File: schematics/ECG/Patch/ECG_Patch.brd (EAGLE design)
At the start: 15.7 x 26.7 mm, 10 parts

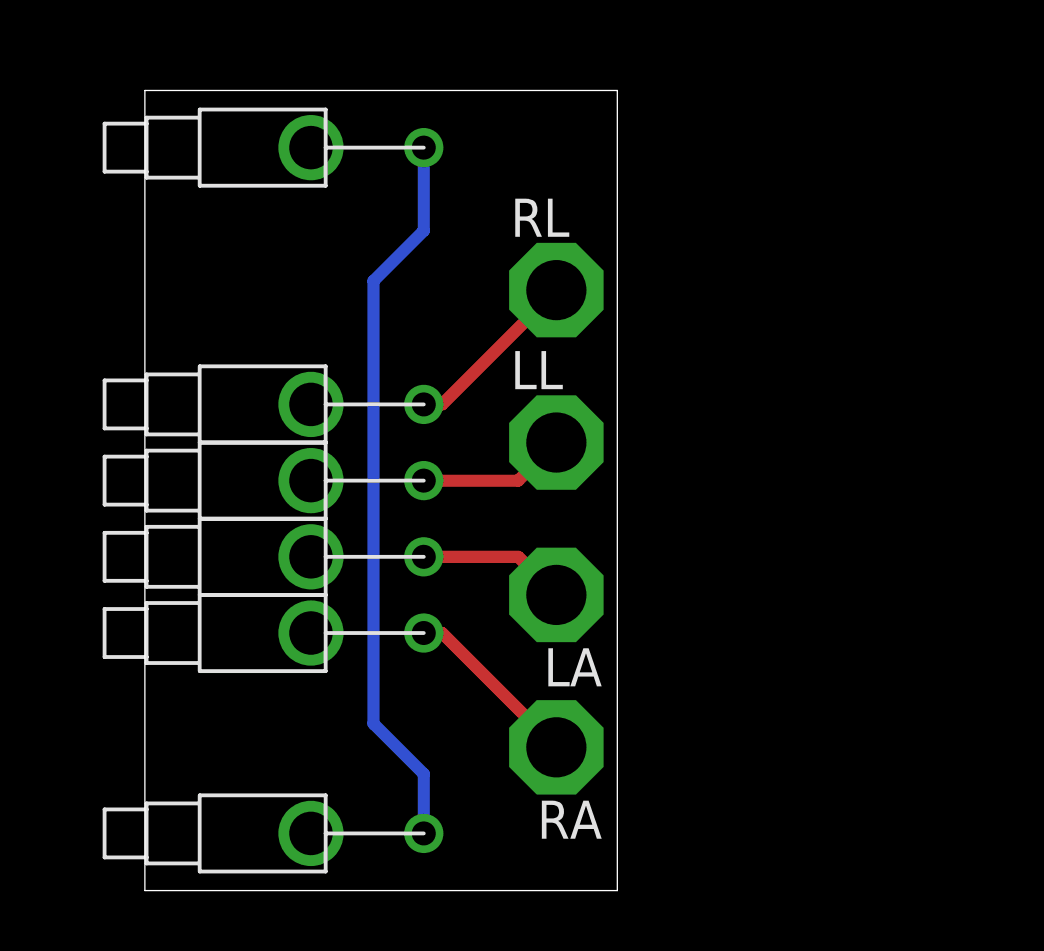
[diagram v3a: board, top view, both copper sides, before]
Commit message: updated all boards to slightly larger dimensions and new target/piston positions
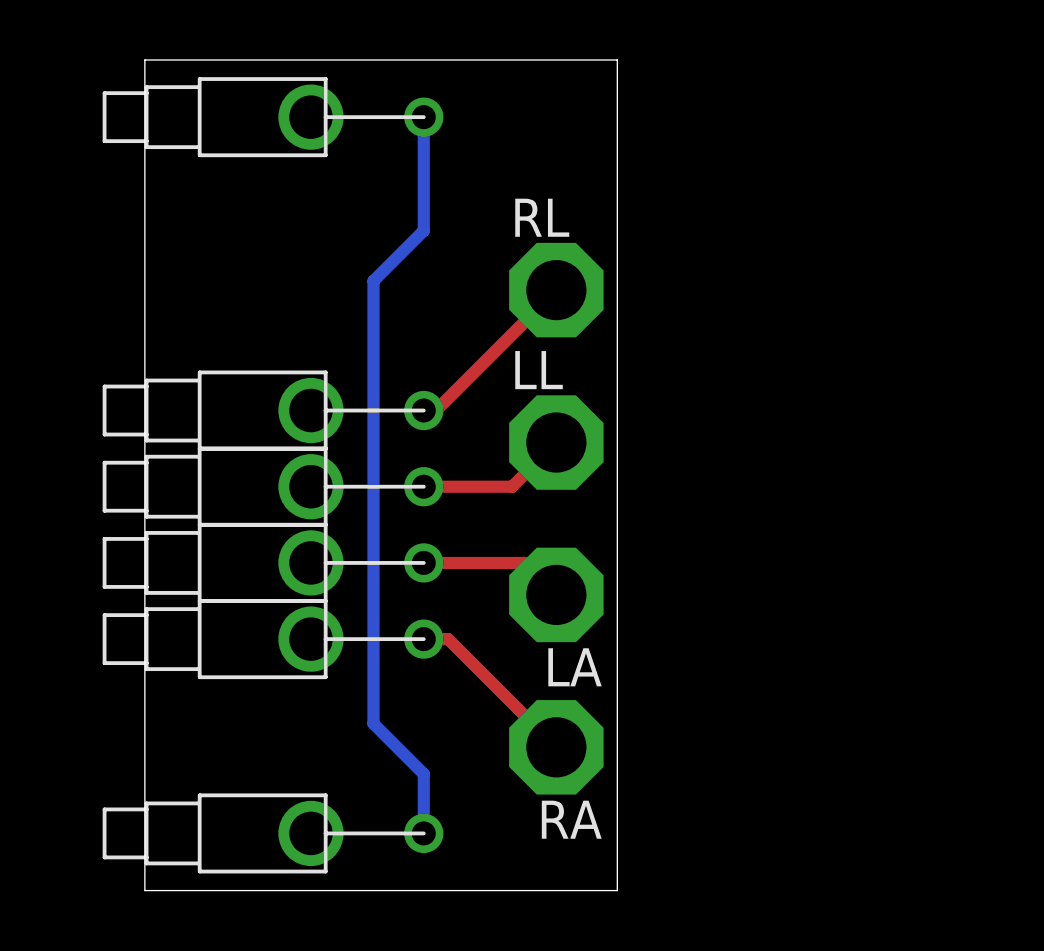
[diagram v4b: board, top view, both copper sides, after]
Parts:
- moved U$5 1.02 mm to (9.30, 25.8)
- moved U$1 0.20 mm to (9.30, 16.0)
- moved U$2 0.20 mm to (9.30, 13.5)
- moved U$4 0.20 mm to (9.30, 8.38)
- moved U$3 0.20 mm to (9.30, 10.9)
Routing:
- net BATT: track 24.2 -> 25.3 mm
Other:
- board size 15.7 x 26.7 mm -> 15.7 x 27.7 mm
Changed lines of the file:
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@@
 <plain>
 <wire x1="0" y1="0" x2="15.748" y2="0" width="0" layer="20"/>
-<wire x1="15.748" y1="0" x2="15.748" y2="26.67" width="0" layer="20"/>
-<wire x1="15.748" y1="26.67" x2="0" y2="26.67" width="0" layer="20"/>
-<wire x1="0" y1="26.67" x2="0" y2="0" width="0" layer="20"/>
+<wire x1="15.748" y1="0" x2="15.748" y2="27.686" width="0" layer="20"/>
+<wire x1="15.748" y1="27.686" x2="0" y2="27.686" width="0" layer="20"/>
+<wire x1="0" y1="27.686" x2="0" y2="0" width="0" layer="20"/>
 </plain>
 <attributes>
@@
 </autorouter>
 <elements>
-<element name="U$1" library="pins" package="PISTON_RA_TH" value="PISTON_RA_TH" x="9.2964" y="16.2052" rot="R180"/>
-<element name="U$2" library="pins" package="PISTON_RA_TH" value="PISTON_RA_TH" x="9.2964" y="13.6652" rot="R180"/>
-<element name="U$3" library="pins" package="PISTON_RA_TH" value="PISTON_RA_TH" x="9.2964" y="11.1252" rot="R180"/>
-<element name="U$4" library="pins" package="PISTON_RA_TH" value="PISTON_RA_TH" x="9.2964" y="8.5852" rot="R180"/>
+<element name="U$1" library="pins" package="PISTON_RA_TH" value="PISTON_RA_TH" x="9.2964" y="16.002" rot="R180"/>
+<element name="U$2" library="pins" package="PISTON_RA_TH" value="PISTON_RA_TH" x="9.2964" y="13.462" rot="R180"/>
+<element name="U$3" library="pins" package="PISTON_RA_TH" value="PISTON_RA_TH" x="9.2964" y="10.922" rot="R180"/>
+<element name="U$4" library="pins" package="PISTON_RA_TH" value="PISTON_RA_TH" x="9.2964" y="8.382" rot="R180"/>
 <element name="LL" library="testpad" package="P1-20" value="TPSQPAD1-20" x="13.716" y="14.9352">
 <attribute name="TP_SIGNAL_NAME" value="" x="13.716" y="14.9352" size="1.778" layer="27" display="off"/>
@@
 <attribute name="TP_SIGNAL_NAME" value="" x="13.716" y="4.7752" size="1.778" layer="27" rot="R180" display="off"/>
 </element>
-<element name="U$5" library="pins" package="PISTON_RA_TH" value="PISTON_RA_TH" x="9.2964" y="24.765" rot="R180"/>
+<element name="U$5" library="pins" package="PISTON_RA_TH" value="PISTON_RA_TH" x="9.2964" y="25.781" rot="R180"/>
 <element name="U$6" library="pins" package="PISTON_RA_TH" value="PISTON_RA_TH" x="9.2964" y="1.905" rot="R180"/>
 </elements>
@@
 <contactref element="U$2" pad="1"/>
 <contactref element="LL" pad="TP"/>
-<wire x1="9.2964" y1="13.6652" x2="12.446" y2="13.6652" width="0.4064" layer="1"/>
-<wire x1="12.446" y1="13.6652" x2="13.716" y2="14.9352" width="0.4064" layer="1"/>
+<wire x1="12.2428" y1="13.462" x2="13.716" y2="14.9352" width="0.4064" layer="1"/>
+<wire x1="9.2964" y1="13.462" x2="12.2428" y2="13.462" width="0.4064" layer="1"/>
 </signal>
 <signal name="N$2">
 <contactref element="U$1" pad="1"/>
 <contactref element="RL" pad="TP"/>
-<wire x1="9.2964" y1="16.2052" x2="9.906" y2="16.2052" width="0.4064" layer="1"/>
-<wire x1="9.906" y1="16.2052" x2="13.716" y2="20.0152" width="0.4064" layer="1"/>
+<wire x1="9.7028" y1="16.002" x2="13.716" y2="20.0152" width="0.4064" layer="1"/>
+<wire x1="9.2964" y1="16.002" x2="9.7028" y2="16.002" width="0.4064" layer="1"/>
 </signal>
 <signal name="N$3">
 <contactref element="U$3" pad="1"/>
 <contactref element="LA" pad="TP"/>
-<wire x1="9.2964" y1="11.1252" x2="12.446" y2="11.1252" width="0.4064" layer="1"/>
-<wire x1="12.446" y1="11.1252" x2="13.716" y2="9.8552" width="0.4064" layer="1"/>
+<wire x1="9.2964" y1="10.922" x2="12.6492" y2="10.922" width="0.4064" layer="1"/>
+<wire x1="12.6492" y1="10.922" x2="13.716" y2="9.8552" width="0.4064" layer="1"/>
 </signal>
 <signal name="N$4">
 <contactref element="U$4" pad="1"/>
 <contactref element="RA" pad="TP"/>
-<wire x1="9.2964" y1="8.5852" x2="9.906" y2="8.5852" width="0.4064" layer="1"/>
-<wire x1="9.906" y1="8.5852" x2="13.716" y2="4.7752" width="0.4064" layer="1"/>
+<wire x1="9.2964" y1="8.382" x2="10.1092" y2="8.382" width="0.4064" layer="1"/>
+<wire x1="10.1092" y1="8.382" x2="13.716" y2="4.7752" width="0.4064" layer="1"/>
 </signal>
 <signal name="BATT">
 <contactref element="U$5" pad="1"/>
 <contactref element="U$6" pad="1"/>
-<wire x1="9.2964" y1="24.765" x2="9.2964" y2="21.9964" width="0.4064" layer="16"/>
+<wire x1="9.2964" y1="25.781" x2="9.2964" y2="21.9964" width="0.4064" layer="16"/>
 <wire x1="9.2964" y1="21.9964" x2="7.62" y2="20.32" width="0.4064" layer="16"/>
 <wire x1="7.62" y1="20.32" x2="7.62" y2="5.5626" width="0.4064" layer="16"/>

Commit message: scaled down patch pcb. Same dimensions as charger board
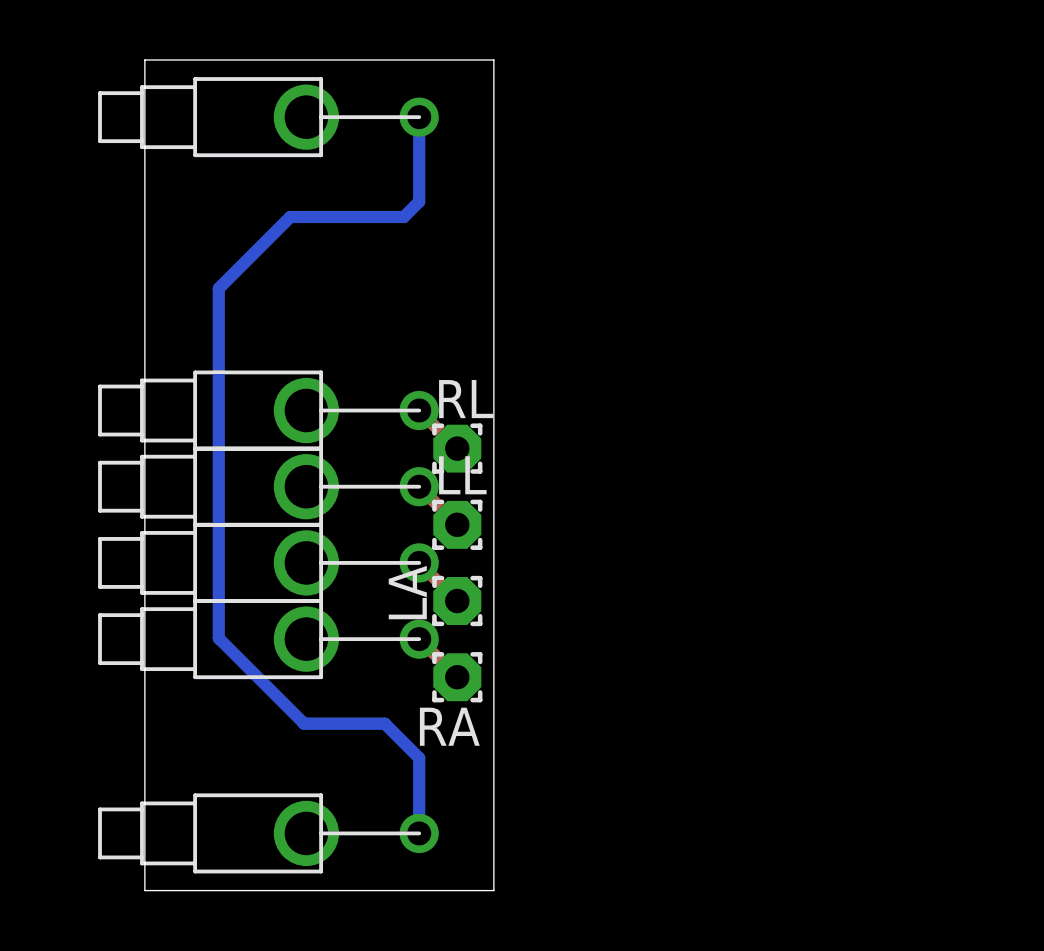
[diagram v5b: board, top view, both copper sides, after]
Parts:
- LA, LL, RA, RL: value TPSQPAD1-20 -> (none); device testpad:P1-20 -> wirepad:1,6/0,8
- moved RL 6.23 mm to (10.4, 14.7)
- moved LL 4.29 mm to (10.4, 12.2)
- moved RA 4.05 mm to (10.4, 7.11)
- moved LA 3.31 mm to (10.4, 9.65), turned to 90 degrees
- moved U$1 0.15 mm to (9.14, 16.0)
- moved U$2 0.15 mm to (9.14, 13.5)
- moved U$3 0.15 mm to (9.14, 10.9)
- moved U$4 0.15 mm to (9.14, 8.38)
- moved U$5 0.15 mm to (9.14, 25.8)
- moved U$6 0.15 mm to (9.14, 1.91)
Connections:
- removed net N$1: LL.TP, U$2.1
- removed net N$2: RL.TP, U$1.1
- removed net N$3: LA.TP, U$3.1
- removed net N$4: RA.TP, U$4.1
- new net LA: LA.1, U$3.1
- new net LL: LL.1, U$2.1
- new net RA: RA.1, U$4.1
- new net RL: RL.1, U$1.1
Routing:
- net BATT: track 25.3 -> 33.2 mm
- net N$2: track 6.08 -> 0.00 mm
- net N$4: track 5.91 -> 0.00 mm
- net N$1: track 5.03 -> 0.00 mm
- net N$3: track 4.86 -> 0.00 mm
- net LA: track 0.00 -> 1.80 mm
- net RL: track 0.00 -> 1.80 mm
- net RA: track 0.00 -> 1.80 mm
- net LL: track 0.00 -> 1.80 mm
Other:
- board size 15.7 x 27.7 mm -> 11.6 x 27.7 mm
- board text added: "ECG PATCH"
- board text added: "LA"
- board text added: "LL"
- board text added: "RA"
- board text added: "RL"
- board text added: "v1.0"
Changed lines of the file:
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@@
 <?xml version="1.0" encoding="utf-8"?>
 <!DOCTYPE eagle SYSTEM "eagle.dtd">
-<eagle version="6.5.0">
+<eagle version="6.4">
 <drawing>
 <settings>
@@
 <layer number="23" name="tOrigins" color="15" fill="1" visible="yes" active="yes"/>
 <layer number="24" name="bOrigins" color="15" fill="1" visible="yes" active="yes"/>
-<layer number="25" name="tNames" color="7" fill="1" visible="yes" active="yes"/>
+<layer number="25" name="tNames" color="7" fill="1" visible="no" active="yes"/>
 <layer number="26" name="bNames" color="7" fill="1" visible="yes" active="yes"/>
 <layer number="27" name="tValues" color="7" fill="1" visible="yes" active="yes"/>
@@
 <board>
 <plain>
-<wire x1="0" y1="0" x2="15.748" y2="0" width="0" layer="20"/>
-<wire x1="15.748" y1="0" x2="15.748" y2="27.686" width="0" layer="20"/>
-<wire x1="15.748" y1="27.686" x2="0" y2="27.686" width="0" layer="20"/>
+<wire x1="0" y1="0" x2="11.6332" y2="0" width="0" layer="20"/>
+<wire x1="11.6332" y1="0" x2="11.6332" y2="27.686" width="0" layer="20"/>
+<wire x1="11.6332" y1="27.686" x2="0" y2="27.686" width="0" layer="20"/>
 <wire x1="0" y1="27.686" x2="0" y2="0" width="0" layer="20"/>
+<text x="8.128" y="14.478" size="0.6096" layer="48">RL</text>
+<text x="8.128" y="11.938" size="0.6096" layer="48">LL</text>
+<text x="8.128" y="9.398" size="0.6096" layer="48">LA</text>
+<text x="8.128" y="6.858" size="0.6096" layer="48">RA</text>
+<text x="11.2776" y="0.9652" size="0.3048" layer="48" rot="R180">ECG PATCH</text>
+<text x="11.2776" y="0.4826" size="0.3048" layer="48" rot="R180">v1.0</text>
 </plain>
 <attributes>
@@
 </autorouter>
 <elements>
-<element name="U$1" library="pins" package="PISTON_RA_TH" value="PISTON_RA_TH" x="9.2964" y="16.002" rot="R180"/>
-<element name="U$2" library="pins" package="PISTON_RA_TH" value="PISTON_RA_TH" x="9.2964" y="13.462" rot="R180"/>
-<element name="U$3" library="pins" package="PISTON_RA_TH" value="PISTON_RA_TH" x="9.2964" y="10.922" rot="R180"/>
-<element name="U$4" library="pins" package="PISTON_RA_TH" value="PISTON_RA_TH" x="9.2964" y="8.382" rot="R180"/>
-<element name="LL" library="testpad" package="P1-20" value="TPSQPAD1-20" x="13.716" y="14.9352">
-<attribute name="TP_SIGNAL_NAME" value="" x="13.716" y="14.9352" size="1.778" layer="27" display="off"/>
-</element>
-<element name="RL" library="testpad" package="P1-20" value="TPSQPAD1-20" x="13.716" y="20.0152">
-<attribute name="TP_SIGNAL_NAME" value="" x="13.716" y="20.0152" size="1.778" layer="27" display="off"/>
-</element>
-<element name="LA" library="testpad" package="P1-20" value="TPSQPAD1-20" x="13.716" y="9.8552" rot="R180">
-<attribute name="TP_SIGNAL_NAME" value="" x="13.716" y="9.8552" size="1.778" layer="27" rot="R180" display="off"/>
-</element>
-<element name="RA" library="testpad" package="P1-20" value="TPSQPAD1-20" x="13.716" y="4.7752" rot="R180">
-<attribute name="TP_SIGNAL_NAME" value="" x="13.716" y="4.7752" size="1.778" layer="27" rot="R180" display="off"/>
-</element>
-<element name="U$5" library="pins" package="PISTON_RA_TH" value="PISTON_RA_TH" x="9.2964" y="25.781" rot="R180"/>
-<element name="U$6" library="pins" package="PISTON_RA_TH" value="PISTON_RA_TH" x="9.2964" y="1.905" rot="R180"/>
+<element name="U$1" library="pins" package="PISTON_RA_TH" value="PISTON_RA_TH" x="9.144" y="16.002" rot="R180"/>
+<element name="U$2" library="pins" package="PISTON_RA_TH" value="PISTON_RA_TH" x="9.144" y="13.462" rot="R180"/>
+<element name="U$3" library="pins" package="PISTON_RA_TH" value="PISTON_RA_TH" x="9.144" y="10.922" rot="R180"/>
+<element name="U$4" library="pins" package="PISTON_RA_TH" value="PISTON_RA_TH" x="9.144" y="8.382" rot="R180"/>
+<element name="U$5" library="pins" package="PISTON_RA_TH" value="PISTON_RA_TH" x="9.144" y="25.781" rot="R180"/>
+<element name="U$6" library="pins" package="PISTON_RA_TH" value="PISTON_RA_TH" x="9.144" y="1.905" rot="R180"/>
+<element name="LL" library="wirepad" package="1,6/0,8" value="" x="10.414" y="12.192"/>
+<element name="RL" library="wirepad" package="1,6/0,8" value="" x="10.414" y="14.732"/>
+<element name="LA" library="wirepad" package="1,6/0,8" value="" x="10.414" y="9.652" rot="R90"/>
+<element name="RA" library="wirepad" package="1,6/0,8" value="" x="10.414" y="7.112" rot="R180"/>
 </elements>
 <signals>
-<signal name="N$1">
+<signal name="LL">
 <contactref element="U$2" pad="1"/>
-<contactref element="LL" pad="TP"/>
-<wire x1="12.2428" y1="13.462" x2="13.716" y2="14.9352" width="0.4064" layer="1"/>
-<wire x1="9.2964" y1="13.462" x2="12.2428" y2="13.462" width="0.4064" layer="1"/>
-</signal>
-<signal name="N$2">
+<contactref element="LL" pad="1"/>
+<wire x1="10.414" y1="12.192" x2="9.144" y2="13.462" width="0.4064" layer="1"/>
+</signal>
+<signal name="RL">
 <contactref element="U$1" pad="1"/>
-<contactref element="RL" pad="TP"/>
-<wire x1="9.7028" y1="16.002" x2="13.716" y2="20.0152" width="0.4064" layer="1"/>
-<wire x1="9.2964" y1="16.002" x2="9.7028" y2="16.002" width="0.4064" layer="1"/>
-</signal>
-<signal name="N$3">
+<contactref element="RL" pad="1"/>
+<wire x1="10.414" y1="14.732" x2="9.144" y2="16.002" width="0.4064" layer="1"/>
+</signal>
+<signal name="LA">
 <contactref element="U$3" pad="1"/>
-<contactref element="LA" pad="TP"/>
-<wire x1="9.2964" y1="10.922" x2="12.6492" y2="10.922" width="0.4064" layer="1"/>
-<wire x1="12.6492" y1="10.922" x2="13.716" y2="9.8552" width="0.4064" layer="1"/>
-</signal>
-<signal name="N$4">
+<contactref element="LA" pad="1"/>
+<wire x1="10.414" y1="9.652" x2="9.144" y2="10.922" width="0.4064" layer="1"/>
+</signal>
+<signal name="RA">
 <contactref element="U$4" pad="1"/>
-<contactref element="RA" pad="TP"/>
-<wire x1="9.2964" y1="8.382" x2="10.1092" y2="8.382" width="0.4064" layer="1"/>
-<wire x1="10.1092" y1="8.382" x2="13.716" y2="4.7752" width="0.4064" layer="1"/>
+<contactref element="RA" pad="1"/>
+<wire x1="10.414" y1="7.112" x2="9.144" y2="8.382" width="0.4064" layer="1"/>
 </signal>
 <signal name="BATT">
 <contactref element="U$5" pad="1"/>
 <contactref element="U$6" pad="1"/>
-<wire x1="9.2964" y1="25.781" x2="9.2964" y2="21.9964" width="0.4064" layer="16"/>
-<wire x1="9.2964" y1="21.9964" x2="7.62" y2="20.32" width="0.4064" layer="16"/>
-<wire x1="7.62" y1="20.32" x2="7.62" y2="5.5626" width="0.4064" layer="16"/>
-<wire x1="7.62" y1="5.5626" x2="9.2964" y2="3.8862" width="0.4064" layer="16"/>
-<wire x1="9.2964" y1="3.8862" x2="9.2964" y2="1.905" width="0.4064" layer="16"/>
+<wire x1="2.4638" y1="20.066" x2="2.4638" y2="8.4074" width="0.4064" layer="16"/>
+<wire x1="2.4638" y1="8.4074" x2="5.3086" y2="5.5626" width="0.4064" layer="16"/>
+<wire x1="9.144" y1="1.905" x2="9.144" y2="4.4196" width="0.4064" layer="16"/>
+<wire x1="9.144" y1="4.4196" x2="8.001" y2="5.5626" width="0.4064" layer="16"/>
+<wire x1="8.001" y1="5.5626" x2="5.3086" y2="5.5626" width="0.4064" layer="16"/>
+<wire x1="9.144" y1="25.781" x2="9.144" y2="22.9616" width="0.4064" layer="16"/>
+<wire x1="9.144" y1="22.9616" x2="8.636" y2="22.4536" width="0.4064" layer="16"/>
+<wire x1="8.636" y1="22.4536" x2="4.8514" y2="22.4536" width="0.4064" layer="16"/>
+<wire x1="4.8514" y1="22.4536" x2="2.4638" y2="20.066" width="0.4064" layer="16"/>
 </signal>
 </signals>
